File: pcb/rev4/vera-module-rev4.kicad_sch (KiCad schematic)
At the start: 109 parts, among them J1 Bus, J2 Prog, J3 SD_Card, J4 Composite, J5 VGA, J6 Conn_01x06_Pin, J9 S-video, U1 ICE40UP5K-SG48ITR50, U10 MIC5504-3.3YM5, U11 THS7314D, U2 74AHC00PW, U3 SN74CBTD3861PWR, U4 74CBTLV3126PW,118, U5 74LVC4245APW, U6 WM8524CGEDT, U7 W25Q16JVSNIQ, U9 AP3417CKTR-G1, X1 SG5032CAN_25.000000M-TJGA3

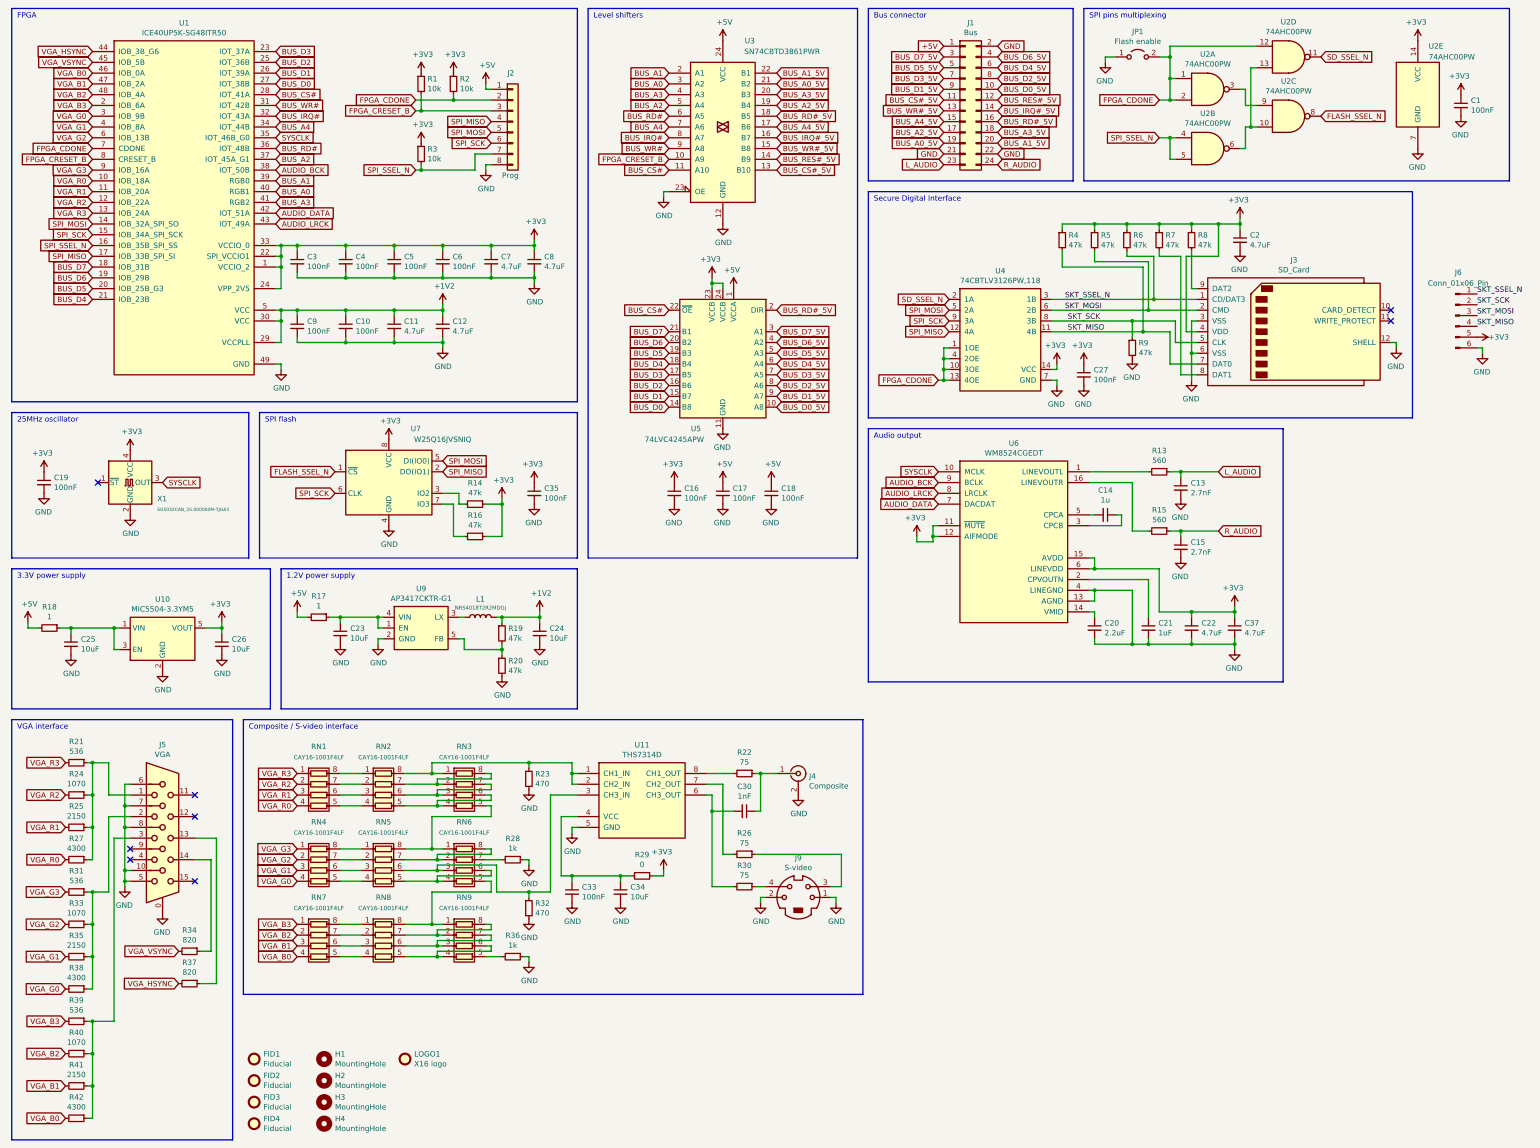
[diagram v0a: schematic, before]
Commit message: ESD protection and HDMI headers
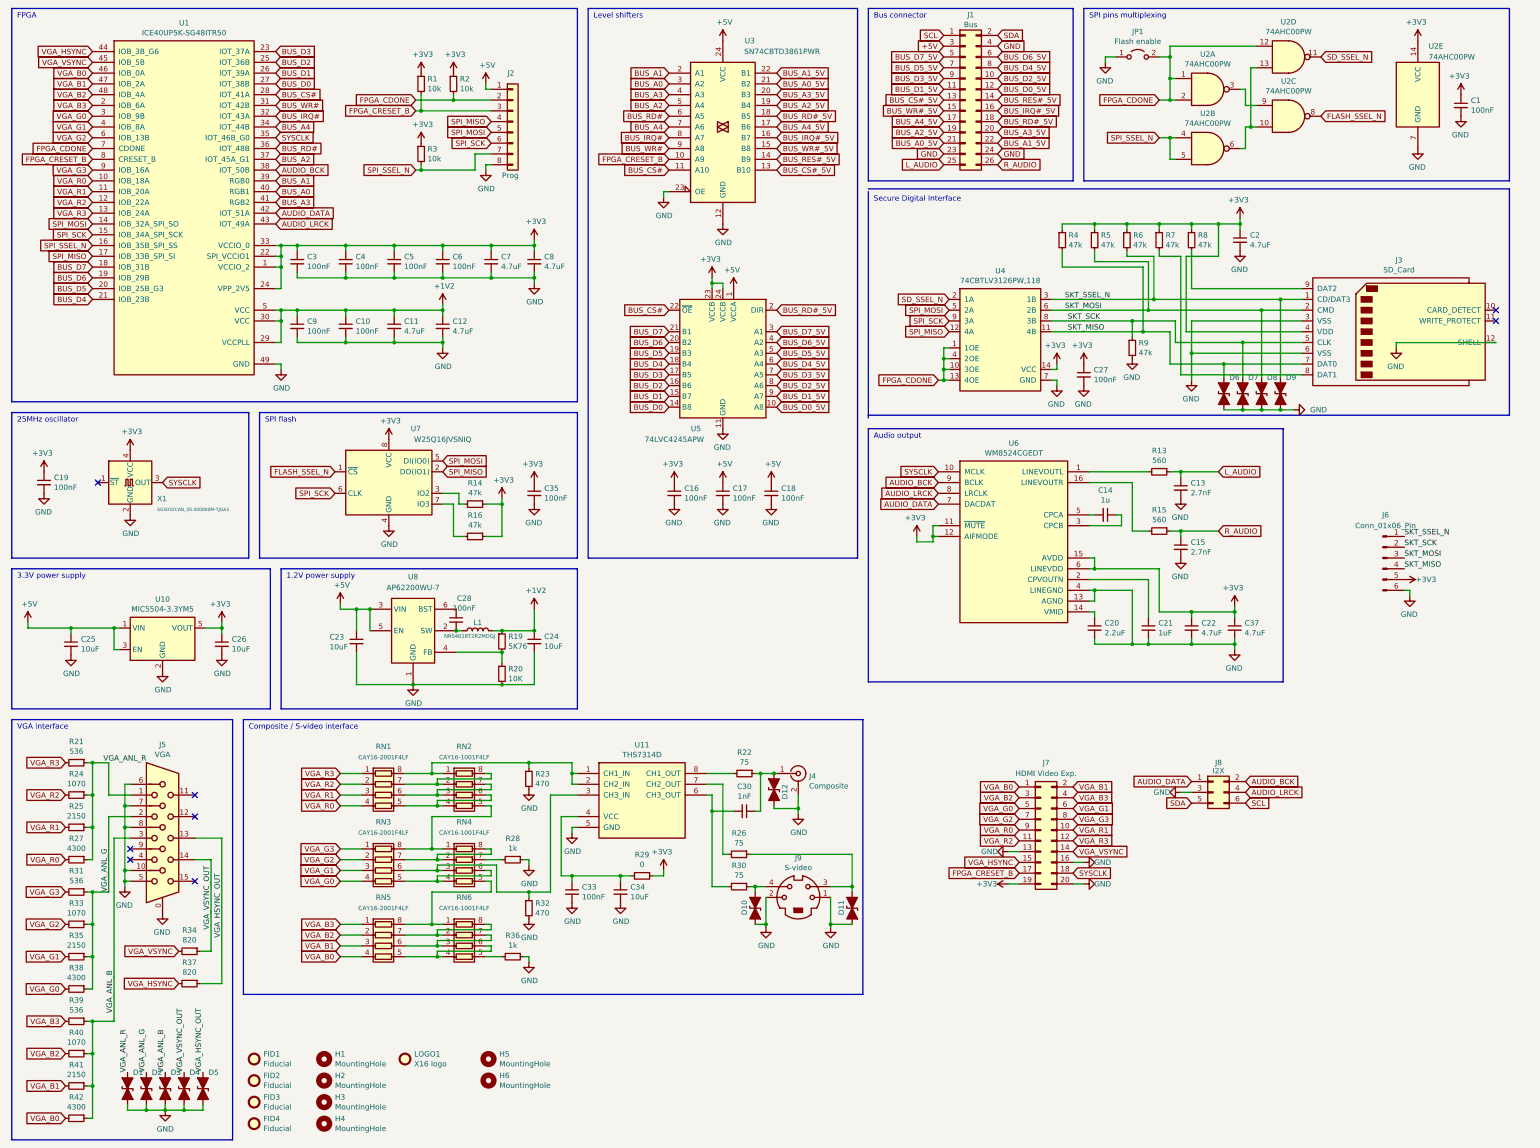
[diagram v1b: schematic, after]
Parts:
- removed R17, R18: 1, Resistor_SMD:R_0603_1608Metric, symbol Device:R_Small
- removed RN1, RN4, RN7: CAY16-1001F4LF, Resistor_SMD:R_Array_Convex_4x0603, symbol Device:R_Pack04
- removed U9: AP3417CKTR-G1, Package_TO_SOT_SMD:SOT-23-5, symbol vera-module:AP3417CKTR-G1
- added C28: 100nF, Capacitor_SMD:C_0603_1608Metric, symbol Device:C_Small
- added D1, D10, D11, D12, D2, D3, D4, D5, D6, D7, D8, D9: D_TVS_Filled, Diode_SMD:D_0603_1608Metric, symbol Device:D_TVS_Filled
- added H5, H6: MountingHole, MountingHole:MountingHole_2.2mm_M2, symbol Mechanical:MountingHole
- added J7: HDMI Video Exp., Connector_PinSocket_2.00mm:PinSocket_2x10_P2.00mm_Vertical_SMD, symbol Connector_Generic:Conn_02x10_Odd_Even
- added J8: I2X, Connector_PinSocket_2.00mm:PinSocket_2x03_P2.00mm_Vertical, symbol Connector_Generic:Conn_02x03_Odd_Even
- added U8: AP62200WU-7, vera-module:TSOT26-6, symbol vera-module:AP62200WU-7
- J1: footprint Connector_PinHeader_2.54mm:PinHeader_2x12_P2.54mm_Vertical -> Connector_PinHeader_2.54mm:PinHeader_2x13_P2.54mm_Vertical; symbol Connector_Generic:Conn_02x12_Odd_Even -> Connector_Generic:Conn_02x13_Odd_Even
- R19: value 47k -> 5K76
- R20: value 47k -> 10K
- RN1: renamed from RN2; value CAY16-1001F4LF -> CAY16-2001F4LF
- RN3: renamed from RN5; value CAY16-1001F4LF -> CAY16-2001F4LF
- RN5: renamed from RN8; value CAY16-1001F4LF -> CAY16-2001F4LF
- renumbered RN3 to RN2, RN6 to RN4, RN9 to RN6
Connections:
- net +3V3: now also J7.19 (Pin_19)
- net +5V: now also C23.1, C25.1, J1.3 (Pin_3), U10.1 (VIN), U10.3 (EN), U8.3 (VIN), U8.5 (EN); no longer J1.1 (Pin_1)
- net AUDIO_BCK: now also J8.2 (Pin_2)
- net AUDIO_DATA: now also J8.1 (Pin_1)
- net AUDIO_LRCK: now also J8.4 (Pin_4)
- net BUS_A0_5V: now also J1.21 (Pin_21); no longer J1.19 (Pin_19)
- net BUS_A1_5V: now also J1.22 (Pin_22); no longer J1.20 (Pin_20)
- net BUS_A2_5V: now also J1.19 (Pin_19); no longer J1.17 (Pin_17)
- net BUS_A3_5V: now also J1.20 (Pin_20); no longer J1.18 (Pin_18)
- net BUS_A4_5V: now also J1.17 (Pin_17); no longer J1.15 (Pin_15)
- net BUS_CS#_5V: now also J1.13 (Pin_13); no longer J1.11 (Pin_11)
- net BUS_D0_5V: now also J1.12 (Pin_12); no longer J1.10 (Pin_10)
- net BUS_D1_5V: now also J1.11 (Pin_11); no longer J1.9 (Pin_9)
- net BUS_D2_5V: now also J1.10 (Pin_10); no longer J1.8 (Pin_8)
- net BUS_D3_5V: now also J1.9 (Pin_9); no longer J1.7 (Pin_7)
- net BUS_D4_5V: now also J1.8 (Pin_8); no longer J1.6 (Pin_6)
- net BUS_D5_5V: now also J1.7 (Pin_7); no longer J1.5 (Pin_5)
- net BUS_D6_5V: now also J1.6 (Pin_6); no longer J1.4 (Pin_4)
- net BUS_D7_5V: now also J1.5 (Pin_5); no longer J1.3 (Pin_3)
- net BUS_IRQ#_5V: now also J1.16 (Pin_16); no longer J1.14 (Pin_14)
- net BUS_RD#_5V: now also J1.18 (Pin_18); no longer J1.16 (Pin_16)
- net BUS_RES#_5V: now also J1.14 (Pin_14); no longer J1.12 (Pin_12)
- net BUS_WR#_5V: now also J1.15 (Pin_15); no longer J1.13 (Pin_13)
- net FPGA_CRESET_B: now also J7.17 (Pin_17)
- net GND: now also J1.23 (Pin_23), J1.24 (Pin_24), J1.4 (Pin_4), D1.1 (A1), D10.1 (A1), D11.1 (A1), D12.1 (A1), D2.1 (A1), D3.1 (A1), D4.1 (A1), D5.1 (A1), D6.1 (A1), D7.1 (A1), D8.1 (A1), D9.1 (A1), J7.13 (Pin_13), J7.16 (Pin_16), J7.20 (Pin_20), J8.3 (Pin_3), U8.1 (GND); no longer J1.2 (Pin_2), J1.21 (Pin_21), J1.22 (Pin_22)
- net L_AUDIO: now also J1.25 (Pin_25); no longer J1.23 (Pin_23)
- net R_AUDIO: now also J1.26 (Pin_26); no longer J1.24 (Pin_24)
- net SKT_MISO: now also D6.2 (A2)
- net SKT_MOSI: now also D8.2 (A2)
- net SKT_SCK: now also D7.2 (A2)
- net SKT_SSEL_N: now also D9.2 (A2)
- net SYSCLK: now also J7.18 (Pin_18)
- net VGA_B0: now also RN5.4 (R4.1), J7.1 (Pin_1)
- net VGA_B1: now also RN5.3 (R3.1), J7.2 (Pin_2)
- net VGA_B2: now also RN5.2 (R2.1), J7.3 (Pin_3)
- net VGA_B3: now also RN5.1 (R1.1), J7.4 (Pin_4)
- net VGA_G0: now also RN3.4 (R4.1), J7.5 (Pin_5)
- net VGA_G1: now also RN3.3 (R3.1), J7.6 (Pin_6)
- net VGA_G2: now also RN3.2 (R2.1), J7.7 (Pin_7)
- net VGA_G3: now also RN3.1 (R1.1), J7.8 (Pin_8)
- net VGA_HSYNC: now also J7.15 (Pin_15)
- net VGA_R0: now also RN1.4 (R4.1), J7.9 (Pin_9)
- net VGA_R1: now also RN1.3 (R3.1), J7.10 (Pin_10)
- net VGA_R2: now also RN1.2 (R2.1), J7.11 (Pin_11)
- net VGA_R3: now also RN1.1 (R1.1), J7.12 (Pin_12)
- net VGA_VSYNC: now also J7.14 (Pin_14)
- net at L1.1: now also C28.2, U8.2 (SW)
- net at R19.2, R20.1: now also U8.4 (FB)
- net VGA_ANL_R: now reaches J5.1, R21.1, R24.1, R25.1, R27.1
- net VGA_ANL_R: now also D1.2 (A2)
- net VGA_HSYNC_OUT: now reaches J5.13, R37.1
- net VGA_HSYNC_OUT: now also D5.2 (A2)
- net VGA_VSYNC_OUT: now reaches J5.14, R34.1
- net VGA_VSYNC_OUT: now also D4.2 (A2)
- net VGA_ANL_G: now reaches J5.2, R31.1, R33.1, R35.1, R38.1
- net VGA_ANL_G: now also D2.2 (A2)
- net VGA_ANL_B: now reaches J5.3, R39.1, R40.1, R41.1, R42.1
- net VGA_ANL_B: now also D3.2 (A2)
- net at C30.1, J4.1 (In), R22.1: now also D12.2 (A2)
- net at J9.3, R26.1: now also D11.2 (A2)
- net at J9.4, R30.1: now also D10.2 (A2)
- new net: C28.1, U8.6 (BST)
- new net SCL: J1.1 (Pin_1), J8.6 (Pin_6)
- new net SDA: J1.2 (Pin_2), J8.5 (Pin_5)
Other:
- moved on the sheet: C23, C24, J3, J6, L1, R19, R20, R26, R30

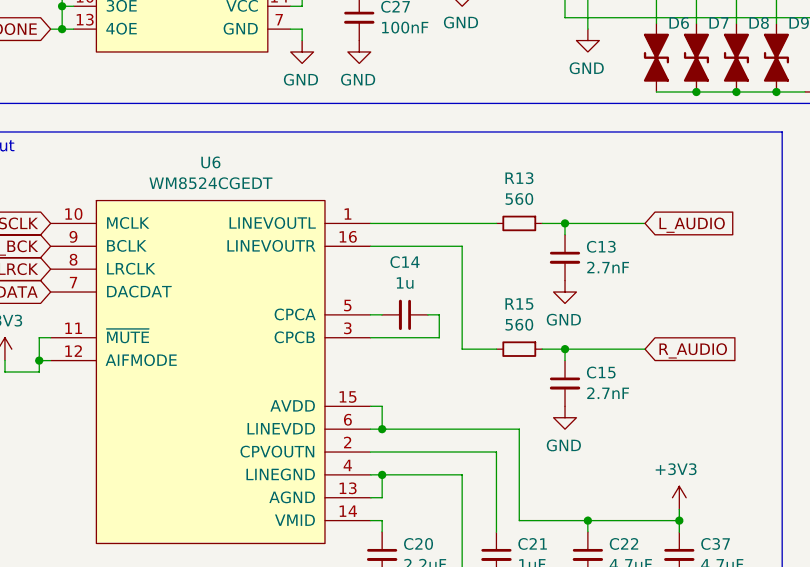
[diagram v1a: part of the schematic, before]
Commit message: Misc panelized PCB changes.
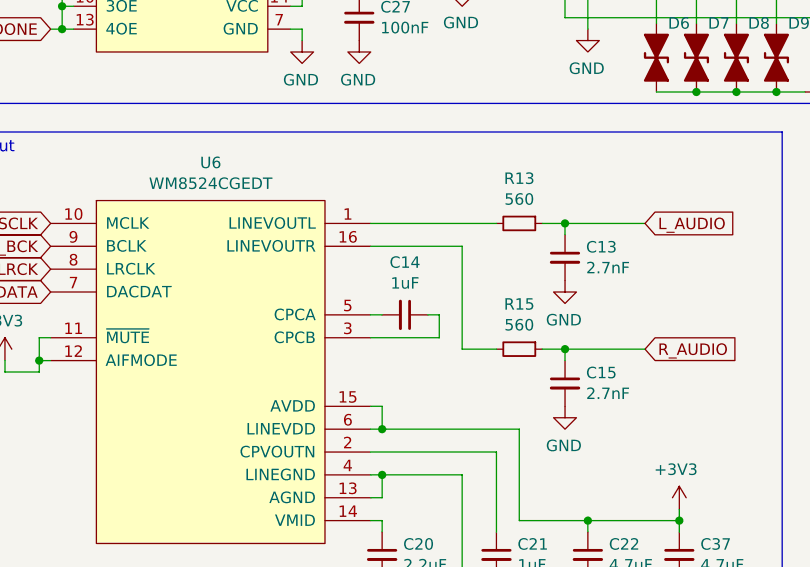
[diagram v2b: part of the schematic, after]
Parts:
- C14: value 1u -> 1uF
- FID1, FID2, FID3, FID4, H1, H2, H3, H4, H5, H6, J7, J8, LOGO1: now left out of the parts list
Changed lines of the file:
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@@
   )
   (symbol (lib_id "Mechanical:Fiducial") (at 107.95 262.89 0) (unit 1)
-    (in_bom yes) (on_board yes) (dnp no)
+    (in_bom no) (on_board yes) (dnp no)
     (property "Reference" "LOGO1" (at 110.109 261.7216 0)
       (effects (font (size 1.27 1.27)) (justify left))
@@
       (effects (font (size 1.27 1.27)))
     )
-    (property "Value" "1u" (at 273.05 131.1148 90)
+    (property "Value" "1uF" (at 273.05 131.1148 90)
       (effects (font (size 1.27 1.27)))
     )
@@
   )
   (symbol (lib_id "Mechanical:Fiducial") (at 72.39 262.89 0) (unit 1)
-    (in_bom yes) (on_board yes) (dnp no)
+    (in_bom no) (on_board yes) (dnp no)
     (property "Reference" "FID1" (at 74.549 261.7216 0)
       (effects (font (size 1.27 1.27)) (justify left))
@@
   )
   (symbol (lib_id "Mechanical:Fiducial") (at 72.39 267.97 0) (unit 1)
-    (in_bom yes) (on_board yes) (dnp no)
+    (in_bom no) (on_board yes) (dnp no)
     (property "Reference" "FID2" (at 74.549 266.8016 0)
       (effects (font (size 1.27 1.27)) (justify left))
@@
   )
   (symbol (lib_id "Mechanical:Fiducial") (at 72.39 273.05 0) (unit 1)
-    (in_bom yes) (on_board yes) (dnp no)
+    (in_bom no) (on_board yes) (dnp no)
     (property "Reference" "FID3" (at 74.549 271.8816 0)
       (effects (font (size 1.27 1.27)) (justify left))
@@
   )
   (symbol (lib_id "Mechanical:Fiducial") (at 72.39 278.13 0) (unit 1)
-    (in_bom yes) (on_board yes) (dnp no)
+    (in_bom no) (on_board yes) (dnp no)
     (property "Reference" "FID4" (at 74.549 276.9616 0)
       (effects (font (size 1.27 1.27)) (justify left))
@@
   )
   (symbol (lib_id "Mechanical:MountingHole") (at 88.9 262.89 0) (unit 1)
-    (in_bom yes) (on_board yes) (dnp no)
+    (in_bom no) (on_board yes) (dnp no)
     (property "Reference" "H1" (at 91.44 261.7216 0)
       (effects (font (size 1.27 1.27)) (justify left))
@@
   )
   (symbol (lib_id "Mechanical:MountingHole") (at 88.9 267.97 0) (unit 1)
-    (in_bom yes) (on_board yes) (dnp no)
+    (in_bom no) (on_board yes) (dnp no)
     (property "Reference" "H2" (at 91.44 266.8016 0)
       (effects (font (size 1.27 1.27)) (justify left))
@@
   )
   (symbol (lib_id "Mechanical:MountingHole") (at 88.9 273.05 0) (unit 1)
-    (in_bom yes) (on_board yes) (dnp no)
+    (in_bom no) (on_board yes) (dnp no)
     (property "Reference" "H3" (at 91.44 271.8816 0)
       (effects (font (size 1.27 1.27)) (justify left))
@@
   )
   (symbol (lib_id "Mechanical:MountingHole") (at 88.9 278.13 0) (unit 1)
-    (in_bom yes) (on_board yes) (dnp no)
+    (in_bom no) (on_board yes) (dnp no)
     (property "Reference" "H4" (at 91.44 276.9616 0)
       (effects (font (size 1.27 1.27)) (justify left))
@@
   )
   (symbol (lib_id "Mechanical:MountingHole") (at 127.635 262.89 0) (unit 1)
-    (in_bom yes) (on_board yes) (dnp no)
+    (in_bom no) (on_board yes) (dnp no)
     (property "Reference" "H5" (at 130.175 261.7216 0)
       (effects (font (size 1.27 1.27)) (justify left))
@@
   )
   (symbol (lib_id "Connector_Generic:Conn_02x10_Odd_Even") (at 257.81 208.915 0) (unit 1)
-    (in_bom yes) (on_board yes) (dnp no) (fields_autoplaced)
+    (in_bom no) (on_board yes) (dnp no) (fields_autoplaced)
     (property "Reference" "J7" (at 259.08 193.04 0)
       (effects (font (size 1.27 1.27)))
@@
   )
   (symbol (lib_id "Mechanical:MountingHole") (at 127.635 267.97 0) (unit 1)
-    (in_bom yes) (on_board yes) (dnp no)
+    (in_bom no) (on_board yes) (dnp no)
     (property "Reference" "H6" (at 130.175 266.8016 0)
       (effects (font (size 1.27 1.27)) (justify left))
@@
   )
   (symbol (lib_id "Connector_Generic:Conn_02x03_Odd_Even") (at 298.45 200.025 0) (unit 1)
-    (in_bom yes) (on_board yes) (dnp no)
+    (in_bom no) (on_board yes) (dnp no)
     (property "Reference" "J8" (at 299.72 193.04 0)
       (effects (font (size 1.27 1.27)))
